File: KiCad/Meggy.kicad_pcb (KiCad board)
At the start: 4 copper layers, 17.4 x 54 mm, 3 parts, among them U1 ROM-42pin, U2 AT90USB1286-MU

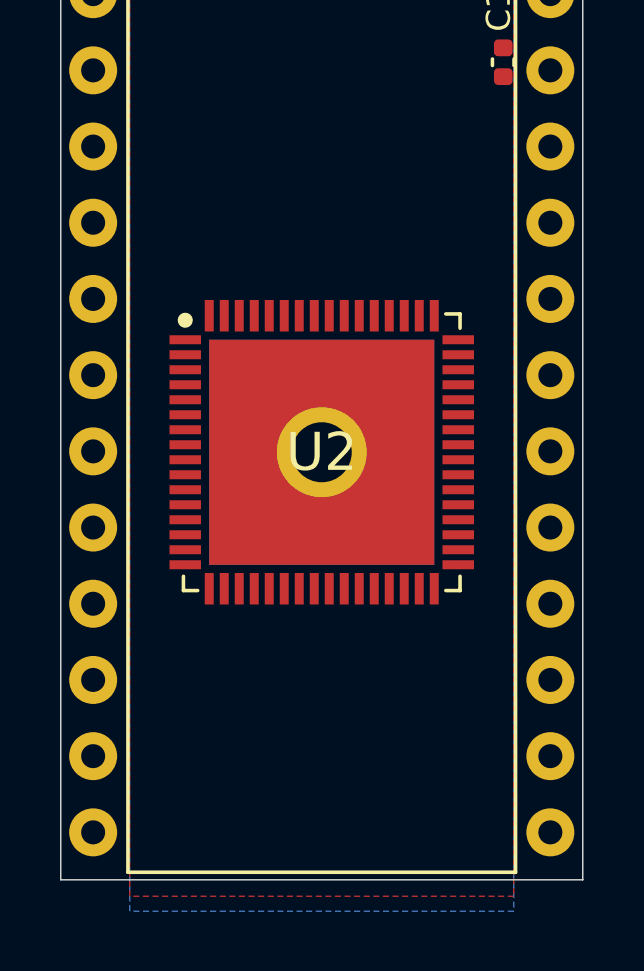
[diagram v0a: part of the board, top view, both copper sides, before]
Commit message: Add Micro USB connector and resistors R1-R3
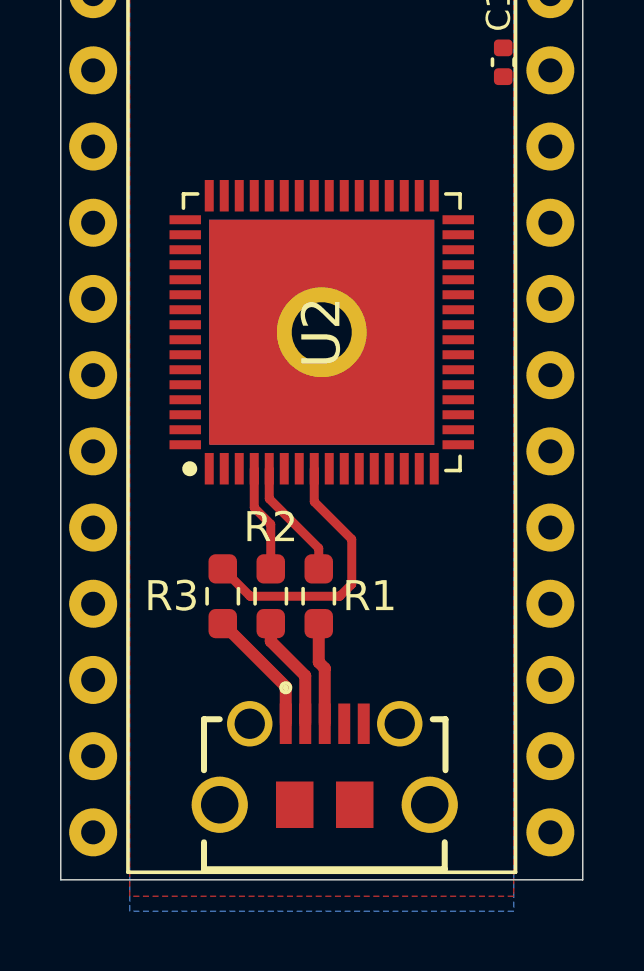
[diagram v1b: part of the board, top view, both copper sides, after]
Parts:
- added J1: USB_B_Micro, Meggy:101181940001LF, F.Cu at (132.1, 108.4)
- added R1: 22, Resistor_SMD:R_0603_1608Metric_Pad0.98x0.95mm_HandSolder, F.Cu at (131.9, 101.8)
- added R2: 22, Resistor_SMD:R_0603_1608Metric_Pad0.98x0.95mm_HandSolder, F.Cu at (130.3, 101.8)
- added R3: 100Ω, Resistor_SMD:R_0603_1608Metric_Pad0.98x0.95mm_HandSolder, F.Cu at (128.7, 101.8)
- U1: value ROM-42pin -> ROM-socket-42pin
- moved U2 4.00 mm to (132.0, 93.0), turned to 90 degrees
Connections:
- net Net-(U1-Pad32) renamed BYTE
- net Net-(U2-Pad24) renamed CLK16M
- U1 pad 12: Net-(U1-Pad12) -> GND
- U1 pad 22: Net-(U1-Pad22) -> VCC
- U1 pad 31: Net-(U1-Pad31) -> GND
- U2 pad 4: Net-(U2-Pad4) -> D-
- U2 pad 5: Net-(U2-Pad5) -> D+
- U2 pad 65: Net-(U2-Pad65) -> GND
- U2 pad 8: Net-(U2-Pad8) -> /VBUS
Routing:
- net /VBUS: track 0.00 -> 9.21 mm
- net /VBUS_5V: track 0.00 -> 4.21 mm
- net D+: track 0.00 -> 4.02 mm
- net Net-(J1-Pad2): track 0.00 -> 3.81 mm
- net D-: track 0.00 -> 3.57 mm
- net Net-(J1-Pad3): track 0.00 -> 3.42 mm

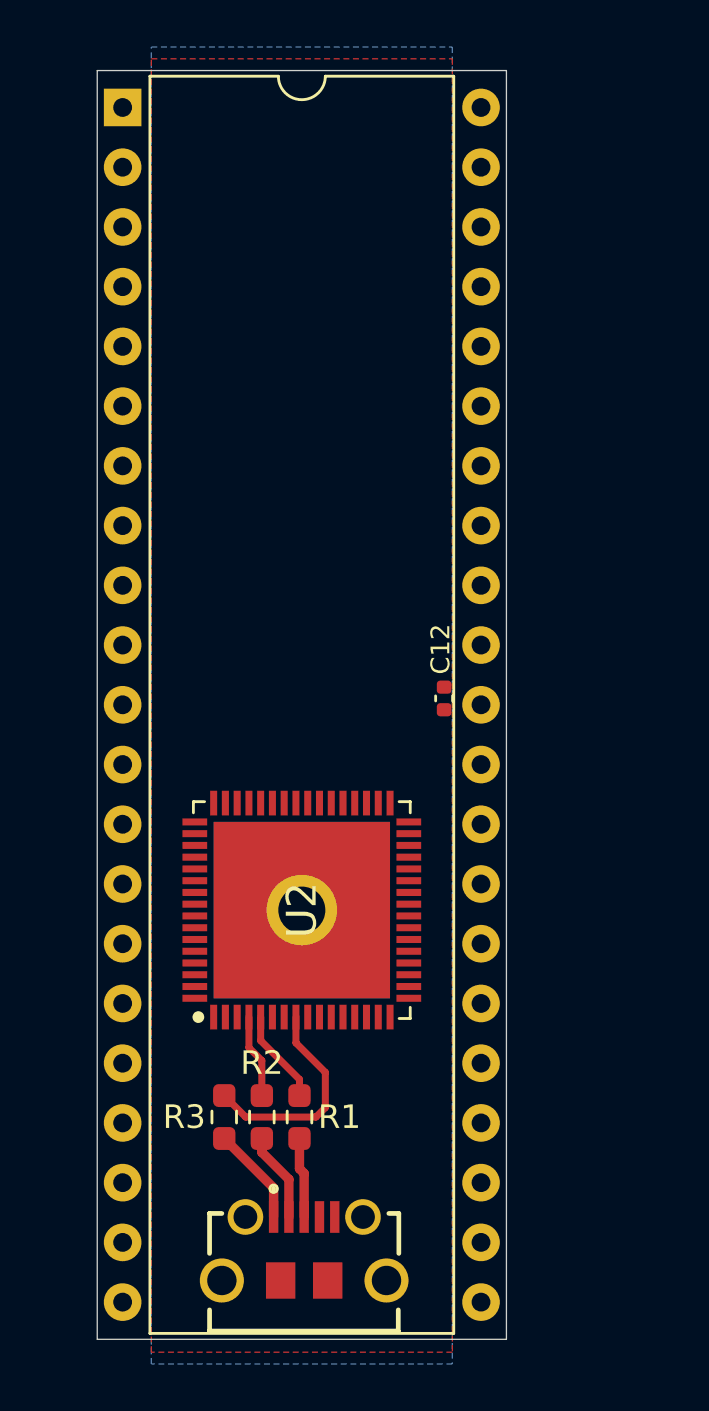
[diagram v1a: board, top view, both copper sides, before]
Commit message: Add U3 M29F160F, pin assignment and preliminary routing
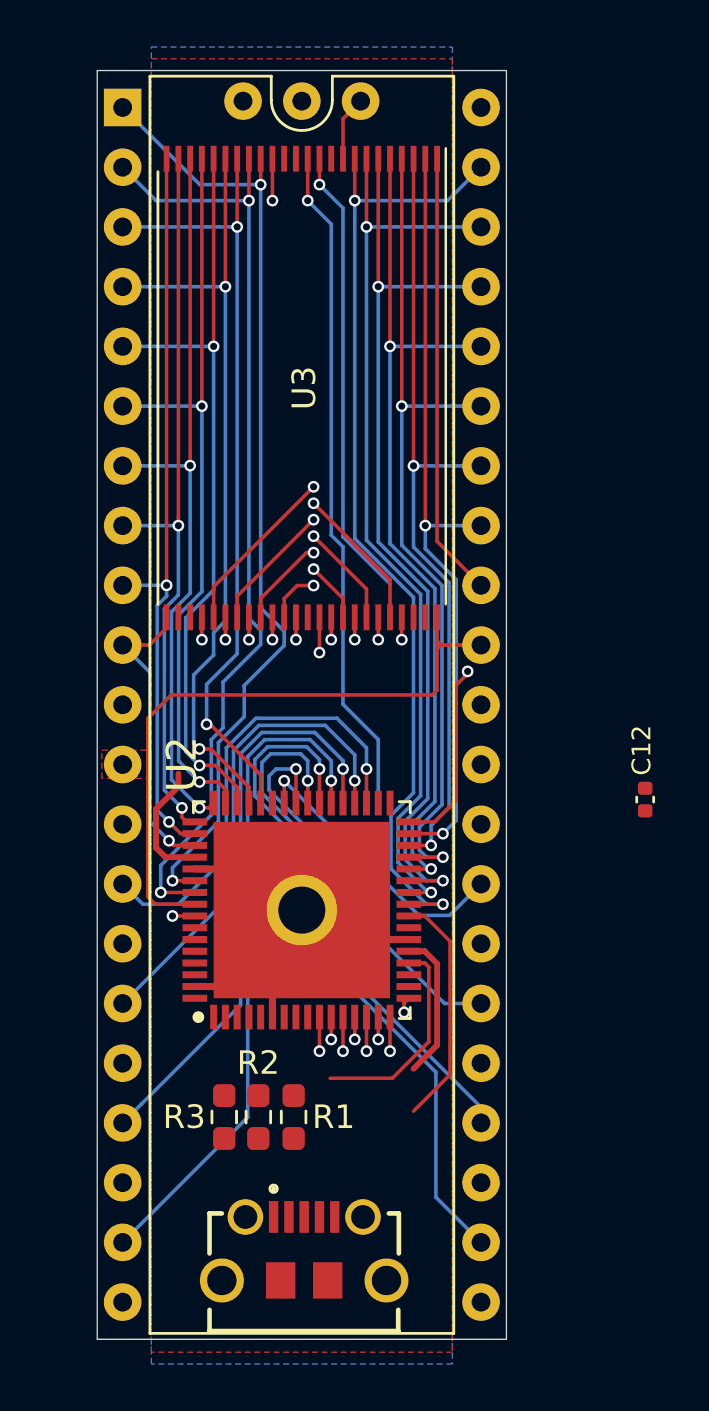
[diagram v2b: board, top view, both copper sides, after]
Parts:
- added J2: Conn_01x03, Connector_PinHeader_2.54mm:PinHeader_1x03_P2.54mm_Vertical, F.Cu at (132.0, 58.6)
- added U3: M29F160F, Package_SO:TSOP-I-48_18.4x12mm_P0.5mm, F.Cu at (132.0, 70.8)
- R3: value 100Ω -> 100
- moved C12 9.57 mm to (146.6, 88.3)
- moved R1 0.25 mm to (131.7, 101.8)
- moved R2 0.15 mm to (130.2, 101.8)
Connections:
- net D+ renamed /D+
- net D- renamed /D-
- net Net-(U1-Pad13) renamed OE_SOCKET
- net Net-(U2-Pad1) renamed PE6
- net Net-(U2-Pad18) renamed PE4
- net Net-(U2-Pad19) renamed PE5
- net Net-(U2-Pad2) renamed PE7
- net Net-(U2-Pad20) renamed RESET
- net Net-(U2-Pad23) renamed XTAL2
- net Net-(U2-Pad33) renamed PE0
- net Net-(U2-Pad34) renamed PE1
- net Net-(U2-Pad43) renamed HWB
- net Net-(U2-Pad58) renamed PF3
- net Net-(U2-Pad59) renamed PF2
- net Net-(U2-Pad60) renamed PF1
- net Net-(U2-Pad61) renamed PF0
- net Net-(U2-Pad62) renamed AREF
- net Net-(U2-Pad7) renamed UCAP
- net Net-(U2-Pad9) renamed PE3
- U1 pad 1: Net-(U1-Pad1) -> A18
- U1 pad 10: Net-(U1-Pad10) -> A0
- U1 pad 11: Net-(U1-Pad11) -> NC
- U1 pad 14: Net-(U1-Pad14) -> D0
- U1 pad 15: Net-(U1-Pad15) -> D8
- U1 pad 16: Net-(U1-Pad16) -> D1
- U1 pad 17: Net-(U1-Pad17) -> D9
- U1 pad 18: Net-(U1-Pad18) -> D2
- U1 pad 19: Net-(U1-Pad19) -> D10
- U1 pad 2: Net-(U1-Pad2) -> A17
- U1 pad 20: Net-(U1-Pad20) -> D3
- U1 pad 21: Net-(U1-Pad21) -> D11
- U1 pad 23: Net-(U1-Pad23) -> D4
- U1 pad 24: Net-(U1-Pad24) -> D12
- U1 pad 25: Net-(U1-Pad25) -> D5
- U1 pad 26: Net-(U1-Pad26) -> D13
- U1 pad 27: Net-(U1-Pad27) -> D6
- U1 pad 28: Net-(U1-Pad28) -> D14
- U1 pad 29: Net-(U1-Pad29) -> D7
- U1 pad 3: Net-(U1-Pad3) -> A7
- U1 pad 30: Net-(U1-Pad30) -> D15
- U1 pad 32: BYTE -> NC
- U1 pad 33: Net-(U1-Pad33) -> A16
- U1 pad 34: Net-(U1-Pad34) -> A15
- U1 pad 35: Net-(U1-Pad35) -> A14
- U1 pad 36: Net-(U1-Pad36) -> A13
- U1 pad 37: Net-(U1-Pad37) -> A12
- U1 pad 38: Net-(U1-Pad38) -> A11
- U1 pad 39: Net-(U1-Pad39) -> A10
- U1 pad 4: Net-(U1-Pad4) -> A6
- U1 pad 40: Net-(U1-Pad40) -> A9
- U1 pad 41: Net-(U1-Pad41) -> A8
- U1 pad 42: (no net) -> NC
- U1 pad 5: Net-(U1-Pad5) -> A5
- U1 pad 6: Net-(U1-Pad6) -> A4
- U1 pad 7: Net-(U1-Pad7) -> A3
- U1 pad 8: Net-(U1-Pad8) -> A2
- U1 pad 9: Net-(U1-Pad9) -> A1
- U2 pad 10: Net-(U2-Pad10) -> D8
- U2 pad 11: Net-(U2-Pad11) -> D9
- U2 pad 12: Net-(U2-Pad12) -> D10
- U2 pad 13: Net-(U2-Pad13) -> D11
- U2 pad 14: Net-(U2-Pad14) -> D12
- U2 pad 15: Net-(U2-Pad15) -> D13
- U2 pad 16: Net-(U2-Pad16) -> D14
- U2 pad 17: Net-(U2-Pad17) -> D15
- U2 pad 21: Net-(U2-Pad21) -> BOARD_5V
- U2 pad 22: Net-(U2-Pad22) -> GND
- U2 pad 25: Net-(U2-Pad25) -> A8
- U2 pad 26: Net-(U2-Pad26) -> A9
- U2 pad 27: Net-(U2-Pad27) -> A10
- U2 pad 28: Net-(U2-Pad28) -> A11
- U2 pad 29: Net-(U2-Pad29) -> A12
- U2 pad 3: Net-(U2-Pad3) -> BOARD_5V
- U2 pad 30: Net-(U2-Pad30) -> A13
- U2 pad 31: Net-(U2-Pad31) -> A14
- U2 pad 32: Net-(U2-Pad32) -> A15
- U2 pad 35: Net-(U2-Pad35) -> D0
- U2 pad 36: Net-(U2-Pad36) -> D1
- U2 pad 37: Net-(U2-Pad37) -> D2
- U2 pad 38: Net-(U2-Pad38) -> D3
- U2 pad 39: Net-(U2-Pad39) -> D4
- U2 pad 40: Net-(U2-Pad40) -> D5
- U2 pad 41: Net-(U2-Pad41) -> D6
- U2 pad 42: Net-(U2-Pad42) -> D7
- U2 pad 44: Net-(U2-Pad44) -> A7
- U2 pad 45: Net-(U2-Pad45) -> A6
- U2 pad 46: Net-(U2-Pad46) -> A5
- U2 pad 47: Net-(U2-Pad47) -> A4
- U2 pad 48: Net-(U2-Pad48) -> A3
- U2 pad 49: Net-(U2-Pad49) -> A2
- U2 pad 50: Net-(U2-Pad50) -> A1
- U2 pad 51: Net-(U2-Pad51) -> A0
- U2 pad 52: Net-(U2-Pad52) -> BOARD_5V
- U2 pad 53: Net-(U2-Pad53) -> GND
- U2 pad 54: Net-(U2-Pad54) -> A18
- U2 pad 55: Net-(U2-Pad55) -> A17
- U2 pad 56: Net-(U2-Pad56) -> A16
- U2 pad 57: Net-(U2-Pad57) -> RY-BY
- U2 pad 6: Net-(U2-Pad6) -> GND
- U2 pad 63: Net-(U2-Pad63) -> GND
- U2 pad 64: Net-(U2-Pad64) -> BOARD_5V
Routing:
- net A8: track 0.00 -> 41.9 mm, vias 0 -> 2
- net D0: track 0.00 -> 41.5 mm, vias 0 -> 2
- net A18: track 0.00 -> 41.3 mm, vias 0 -> 2
- net A17: track 0.00 -> 40.6 mm, vias 0 -> 2
- net D3: track 0.00 -> 40.2 mm, vias 0 -> 2
- net D1: track 0.00 -> 39.4 mm, vias 0 -> 2
- net D2: track 0.00 -> 39.2 mm, vias 0 -> 2
- net A9: track 0.00 -> 39.0 mm, vias 0 -> 2
- net A10: track 0.00 -> 38.9 mm, vias 0 -> 2
- net D11: track 0.00 -> 36.9 mm, vias 0 -> 2
- net A11: track 0.00 -> 36.6 mm, vias 0 -> 2
- net A12: track 0.00 -> 36.4 mm, vias 0 -> 2
- net D4: track 0.00 -> 36.0 mm, vias 0 -> 2
- net D5: track 0.00 -> 35.7 mm, vias 0 -> 2
- net RY-BY: track 0.00 -> 35.1 mm, vias 0 -> 2
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
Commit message: Add capacitors and a XTAL_OSC plus 22 Ohm resistor for 16MHz clock and more placement and routing
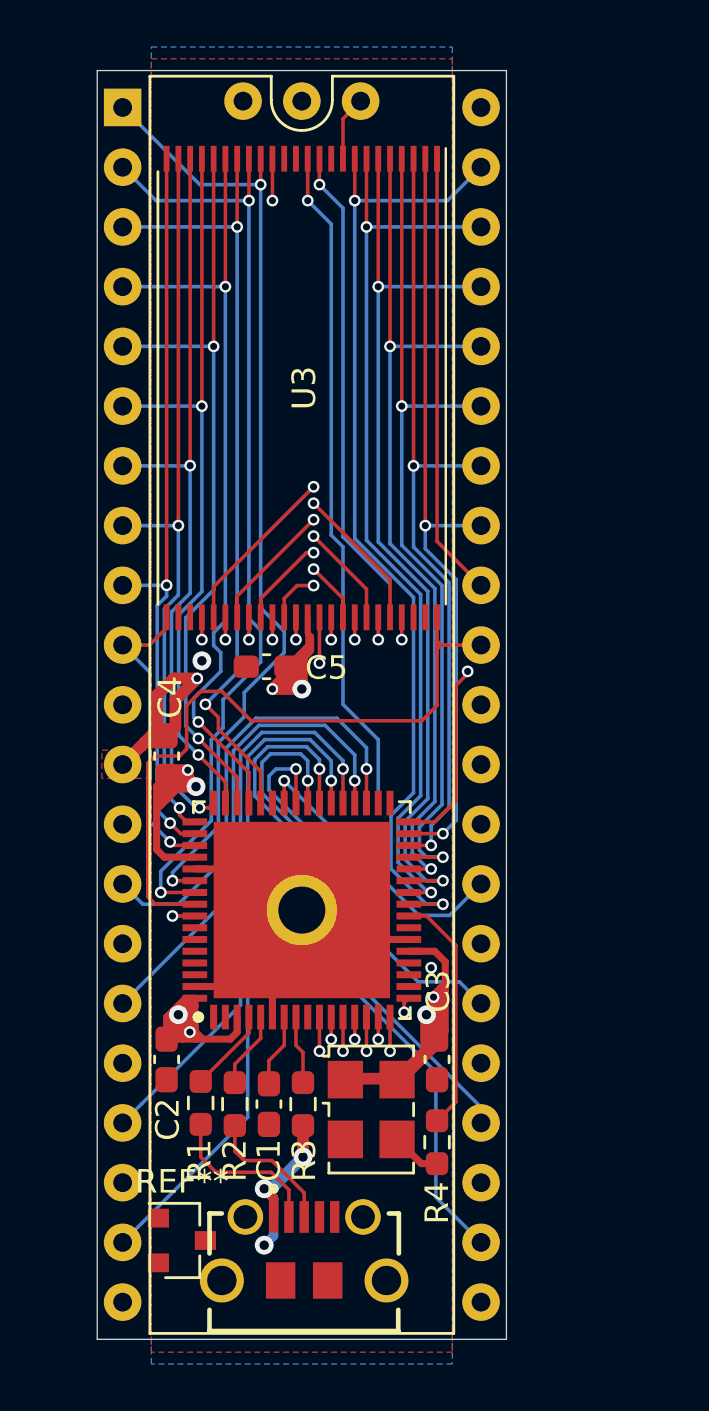
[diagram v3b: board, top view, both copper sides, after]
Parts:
- removed C12: 0.01uF (0402), Capacitor_SMD:C_0402_1005Metric
- removed the R1 at (131.7, 101.8)
- added C1: 1uF, Capacitor_SMD:C_0603_1608Metric_Pad1.08x0.95mm_HandSolder, F.Cu at (130.6, 101.2)
- added C2: 100nF, Capacitor_SMD:C_0603_1608Metric_Pad1.08x0.95mm_HandSolder, F.Cu at (126.2, 99.3)
- added C3: 100nF, Capacitor_SMD:C_0603_1608Metric_Pad1.08x0.95mm_HandSolder, F.Cu at (137.8, 99.3)
- added C4: 100nF, Capacitor_SMD:C_0603_1608Metric_Pad1.08x0.95mm_HandSolder, F.Cu at (126.2, 86.5)
- added C5: 100nF, Capacitor_SMD:C_0603_1608Metric_Pad1.08x0.95mm_HandSolder, F.Cu at (130.5, 82.7)
- added R2: 22, Resistor_SMD:R_0603_1608Metric_Pad0.98x0.95mm_HandSolder, F.Cu at (129.2, 101.2)
- added R4: 22, Resistor_SMD:R_0603_1608Metric_Pad0.98x0.95mm_HandSolder, F.Cu at (137.8, 102.9)
- added REF**: SOT-23, Package_TO_SOT_SMD:SOT-23, F.Cu at (126.9, 107.0)
- added X1: Standard_Clock_Oscillators_XTAL_OSC, Oscillator:Oscillator_SMD_SeikoEpson_SG8002LB-4Pin_5.0x3.2mm, F.Cu at (134.9, 101.5)
- moved R3 3.39 mm to (132.1, 101.2)
- moved R1 2.52 mm to (127.7, 101.2)
- renumbered R2 to R1
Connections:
- U1 pad 11: NC -> NC1
- U1 pad 32: NC -> NC2
- U2 pad 24: CLK16M -> /CLK16M
- U2 pad 7: UCAP -> Net-(C1-Pad1)
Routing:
- net BOARD_5V: track 11.7 -> 67.6 mm, vias 0 -> 8
- net /CLK16M: track 0.00 -> 10.3 mm
- net GND: track 21.3 -> 31.5 mm, vias 0 -> 2
- net CLK16M: track 10.1 -> 0.00 mm
- net RESET: track 8.94 -> 0.00 mm, vias 0 -> 1
- net /VBUS_5V: track 0.00 -> 7.64 mm, vias 0 -> 3
- net Net-(J1-Pad2): track 0.00 -> 6.87 mm
- net Net-(J1-Pad3): track 0.00 -> 5.80 mm
- net /D-: track 0.00 -> 3.59 mm
- net /D+: track 0.00 -> 3.24 mm
- net Net-(C1-Pad1): track 0.00 -> 3.11 mm
- net /VBUS: track 0.00 -> 2.91 mm
- net Net-(R4-Pad2): track 0.00 -> 2.13 mm
- net A16: track 28.2 -> 29.6 mm

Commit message: Added Q1 and Q2 MOSFETs, changed footprint on CLK16M resistor and routed RST and WE signals
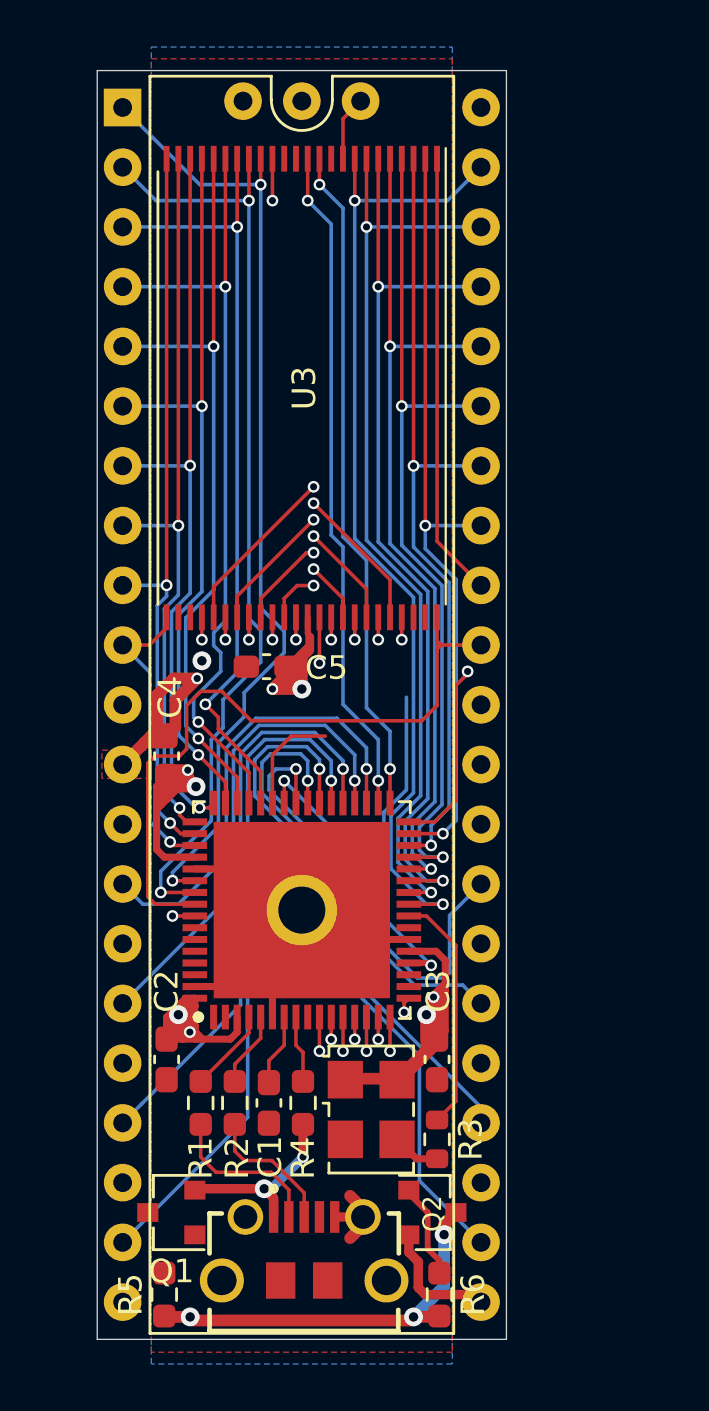
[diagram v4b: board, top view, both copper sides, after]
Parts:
- removed REF**: SOT-23, Package_TO_SOT_SMD:SOT-23
- added Q1: DMP2305U-7, Package_TO_SOT_SMD:SOT-23, F.Cu at (126.5, 105.9)
- added Q2: DMP2305U-7, Package_TO_SOT_SMD:SOT-23, F.Cu at (137.6, 105.9)
- added R5: 100, Resistor_SMD:R_0603_1608Metric_Pad0.98x0.95mm_HandSolder, F.Cu at (126.2, 109.3)
- added R6: 100, Resistor_SMD:R_0603_1608Metric_Pad0.98x0.95mm_HandSolder, F.Cu at (137.8, 109.3)
- R3: renamed from R4; footprint Resistor_SMD:R_0603_1608Metric_Pad0.98x0.95mm_HandSolder -> Resistor_SMD:R_0603_1608Metric
- moved R3 0.12 mm to (137.8, 102.8)
- renumbered R3 to R4
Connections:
- net /VBUS_5V renamed VBUS_5V
- U2 pad 33: PE0 -> WE
- U2 pad 34: PE1 -> RST
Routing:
- net BOARD_5V: track 67.6 -> 84.6 mm, vias 8 -> 11
- net RESET: track 0.00 -> 13.6 mm
- net WE: track 19.3 -> 28.6 mm, vias 1 -> 2
- net VCC: track 0.00 -> 5.33 mm
- net D7: track 32.4 -> 37.6 mm
- net HWB: track 0.00 -> 4.63 mm
- net Net-(Q2-Pad1): track 0.00 -> 4.14 mm
- net GND: track 31.5 -> 35.0 mm
- net D14: track 27.1 -> 28.7 mm
- net D12: track 28.6 -> 30.2 mm
- net D13: track 24.8 -> 26.4 mm
- net D15: track 22.1 -> 21.2 mm
- net RST: track 28.4 -> 28.6 mm, vias 1 -> 2
- net VBUS_5V: track 7.64 -> 7.73 mm, vias 3 -> 2

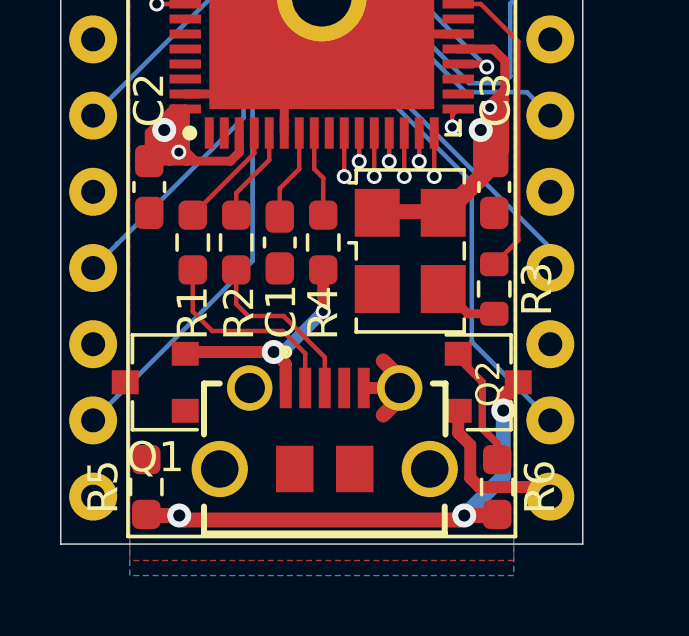
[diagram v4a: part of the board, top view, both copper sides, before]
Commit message: Removed R5,R6 and added D1,D2 changing the 5V Power Protection & ORing Circuit
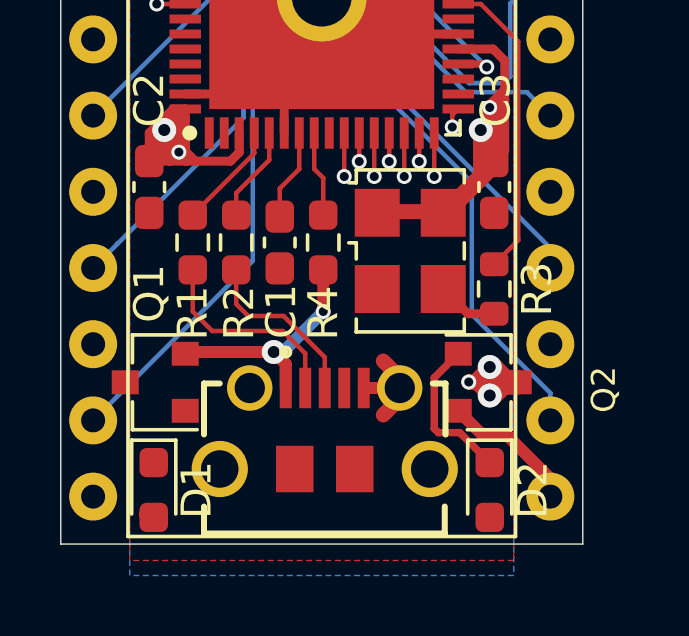
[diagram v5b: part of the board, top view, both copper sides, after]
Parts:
- removed R5, R6: 100, Resistor_SMD:R_0603_1608Metric_Pad0.98x0.95mm_HandSolder
- added D1: MMDL6050T1G, Meggy:D_0603_1608Metric_Pad_0.975x0.95mm_HandSolder, F.Cu at (126.4, 109.5)
- added D2: MMDL6050T1G, Meggy:D_0603_1608Metric_Pad_0.975x0.95mm_HandSolder, F.Cu at (137.6, 109.5)
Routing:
- net BOARD_5V: track 84.6 -> 72.6 mm
- net Net-(D2-Pad1): track 4.14 -> 5.14 mm
- net VCC: track 5.33 -> 4.61 mm
